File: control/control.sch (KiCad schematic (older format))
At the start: 135 parts, among them IC1 TJA1040, IC2 DNP MAX481CSA, IC3 ST232BD, IC4 ATMEGA128-A, IC5 ST232BD, IC6 FT232RL, J4 POWER, P1 SENSOR, P10 DB9, P11 B, P12 USB_4, P13 DB9, P2 I2C0, P3 I2C1, P4 I2C2, P5 COIN, P6 BILL, P7 ISP, P8 CONN_2, P9 CONN_2, X1 16MHz

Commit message: Updated control board for KiCad 4.0
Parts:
- removed P11: B, USB_B, symbol USB_B_5
- removed P12: USB_4, USB_MINI_B_6, symbol USB_MINI_B_6
- added P11: USB_B, Connect:USB_B, symbol USB_B
- added P12: USB_OTG, Connect:USB_Micro-B, symbol USB_OTG
- added R71: DNP, Resistors_SMD:R_0805_HandSoldering, symbol R
- C1, C10, C11, C12, C13, C14, C15, C16, C17, C18, C19, C2, C20, C21, C22, C23, C25, C27, C28, C29, C3, C30, C31, C4, C5, C6, C7, C8, C9: footprint R0805 -> Capacitors_SMD:C_0805_HandSoldering
- C24, C26, C32: footprint C1V5 -> Capacitors_ThroughHole:C_Radial_D5_L11_P2.5; symbol CP1 -> CP
- D1, D2, D3, D4, D5: footprint LED-0805 -> LEDs:LED-0805
- IC1, IC2: footprint SO8N -> Housings_SOIC:SOIC-8_3.9x4.9mm_Pitch1.27mm
- IC3, IC5: footprint SO16N -> Housings_SOIC:SOIC-16_3.9x9.9mm_Pitch1.27mm
- IC4: footprint TQFP64 -> Housings_QFP:TQFP-64_14x14mm_Pitch0.8mm
- IC6: footprint SSOP28 -> Housings_SSOP:SSOP-28_5.3x10.2mm_Pitch0.65mm
- J4: footprint he10-16ds -> Pin_Headers:Pin_Header_Straight_2x08; symbol BUS_I2C -> Bus_I2C
- JP1, JP2: footprint SIL-3 -> Pin_Headers:Pin_Header_Straight_1x03
- L1: footprint wuerth_elektronik_v5-WE-PD2_S -> matemat:wuerth_elektronik_v5-WE-PD2_S
- P1: footprint he10-16ds -> Pin_Headers:Pin_Header_Straight_2x08
- P10, P13: footprint DB9MCS -> matemat:DB9MCS
- P2, P3, P4, P5: footprint he10-10ds -> Pin_Headers:Pin_Header_Straight_2x05
- P6: footprint HE10_26DS -> Pin_Headers:Pin_Header_Straight_2x13
- P7: footprint pin_array_3x2 -> Pin_Headers:Pin_Header_Straight_2x03
- P8: value CONN_2 -> 12V; footprint Bornier_B2_Phoenix -> matemat:Bornier_B2_Phoenix
- P9: value CONN_2 -> 5V; footprint Bornier_B2_Phoenix -> matemat:Bornier_B2_Phoenix
- R1, R10, R11, R12, R13, R14, R15, R16, R17, R18, R19, R2, R20, R21, R22, R23, R24, R25, R26, R27, R28, R29, R3, R30, R31, R32, R33, R34, R35, R36, R37, R38, R39, R4, R40, R41, R42, R43, R44, R45, R46, R47, R48, R49, R5, R50, R51, R52, R53, R54, R55, R56, R57, R58, R59, R6, R60, R61, R62, R63, R64, R65, R66, R67, R68, R69, R7, R70, R8, R9: footprint R0805 -> Resistors_SMD:R_0805_HandSoldering
- TP1, TP2, TP3, TP4: footprint TROU3 -> Mounting_Holes:MountingHole_3mm
- X1: footprint Q_49U3HMS -> Crystals:Q_49U3HMS; symbol CRYSTAL -> Crystal
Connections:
- wire segments 296 -> 281
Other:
- moved on the sheet: C1, C10, C11, C12, C13, C14, C15, C16, C17, C18, C19, C2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

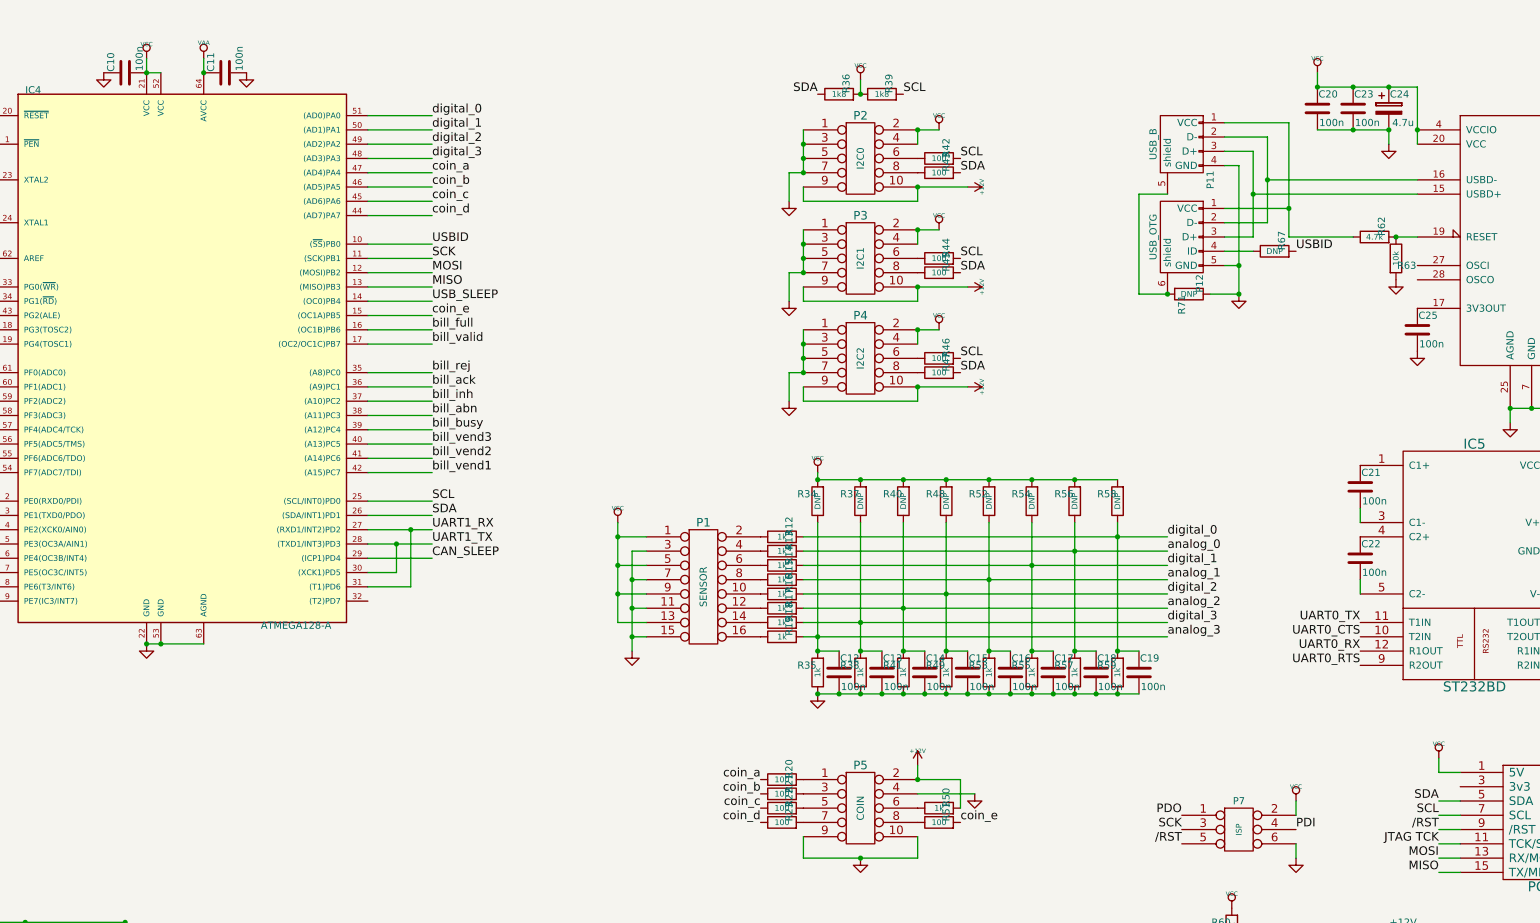
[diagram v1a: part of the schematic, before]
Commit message: Removed pulldown resistors from analog/digital I/O block to save some space. Removed leftover reference from conversion to KiCad 4.
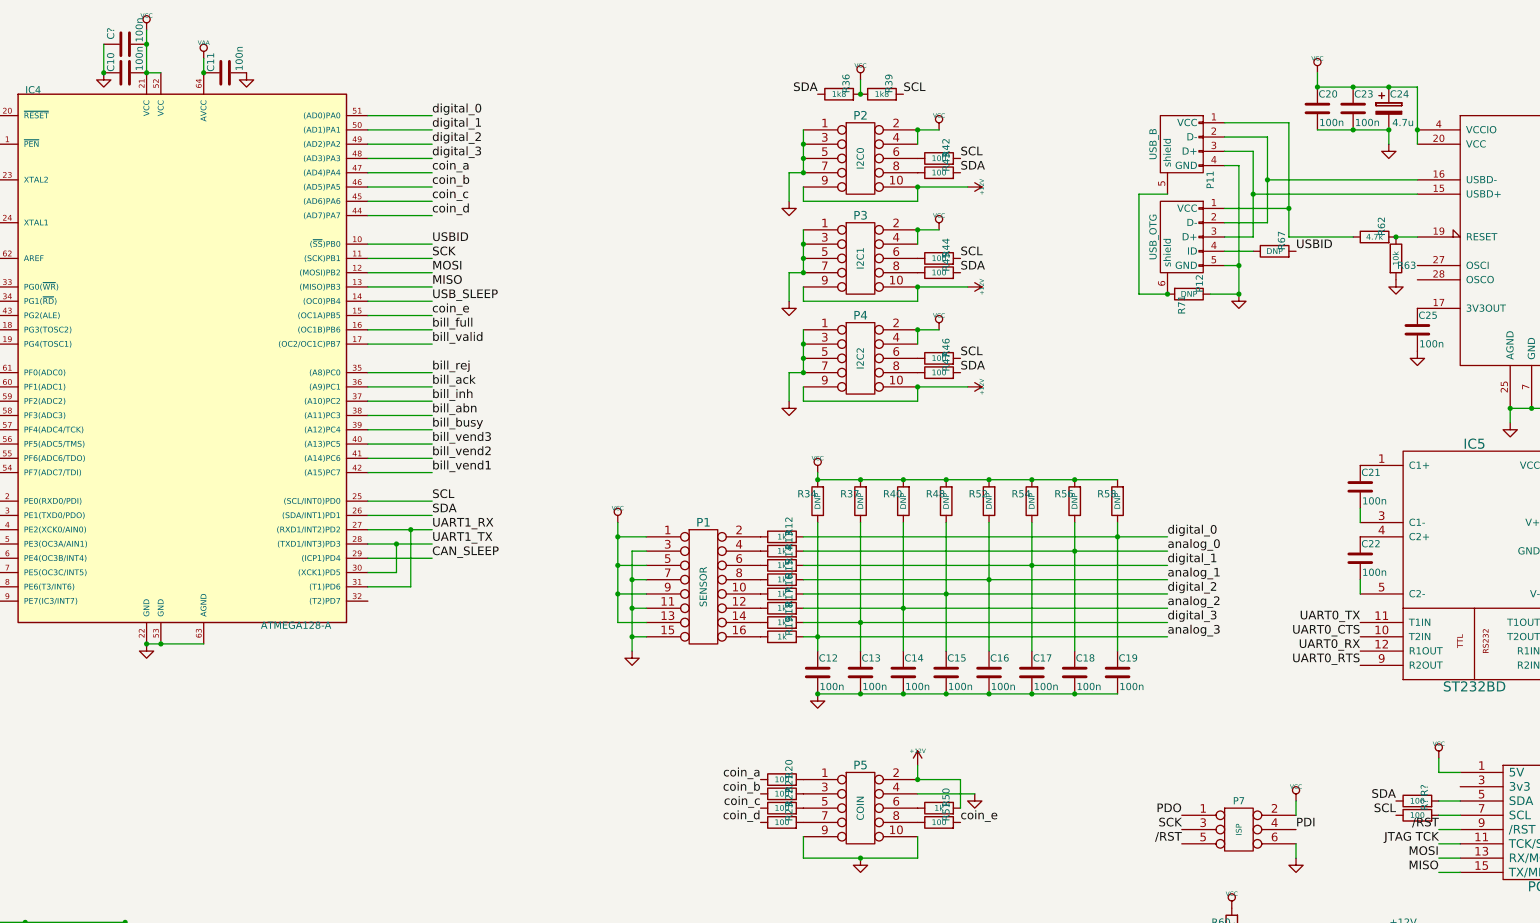
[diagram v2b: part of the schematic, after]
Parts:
- removed R35, R38, R41, R49, R53, R55, R57, R59: 1k, Resistors_SMD:R_0805_HandSoldering, symbol R
- added C?: 100n, Capacitors_SMD:C_0805_HandSoldering, symbol C
- added R? (x2): 100, Resistors_SMD:R_0805_HandSoldering, symbol R
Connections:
- net GND: now also C?.1
- net SCL: now also R?.1; no longer J4.7 (SCL)
- net SDA: now also R?.1; no longer J4.5 (SDA)
- net VCC: now also C?.2
- new net: J4.5 (SDA), R?.2
- new net: J4.7 (SCL), R?.2
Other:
- moved on the sheet: C12, C13, C14, C15, C16, C17, C18, C19

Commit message: Added new connection blocks for coin and banknote scanners
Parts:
- added P?: COIN, symbol CONN_01X17
- added P?: CONN_02X13, symbol CONN_02X13
- added R? (x13): 1k, Resistors_SMD:R_0805_HandSoldering, symbol R
- added R? (x4): 10k, Resistors_SMD:R_0805_HandSoldering, symbol R
- added R? (x2): DNP, Resistors_SMD:R_0805_HandSoldering, symbol R
- added R?: 0, Resistors_SMD:R_0805_HandSoldering, symbol R
- JP2: value 1-2 RESET -> RESET; symbol JUMPER3 -> JUMPER
- R61: value 1k -> 10k
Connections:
- net +12V: now also P?.1 (P1), P?.11 (P11), P?.3 (P3)
- net GND: now also P?.10 (P10), P?.12 (P12), P?.12 (P12), P?.14 (P14), P?.2 (P2), P?.22 (P22), P?.24 (P24), P?.26 (P26), P?.3 (P3), P?.4 (P4), P?.6 (P6), P?.8 (P8), R?.1, R?.1
- net VCC: now also P?.15 (P15), P?.17 (P17), P?.19 (P19), R?.2, R?.2, R?.2, R?.2, R?.2, R?.2, R?.2, R?.2, R?.2, R?.2, R?.2, R?.2, R?.2, R?.2, R?.2, R?.2, R?.2, R?.2
- net /RST renamed ~RST~
- net FLASH_EN renamed ~FLASH_EN~
- net analog_0 renamed ANALOG_0
- net analog_1 renamed ANALOG_1
- net analog_2 renamed ANALOG_2
- net analog_3 renamed ANALOG_3
- net digital_0 renamed DIGITAL_0
- net digital_1 renamed DIGITAL_1
- net digital_2 renamed DIGITAL_2
- net digital_3 renamed DIGITAL_3
- new net BILL_IN_ACK: P?.18 (P18), R?.1
- new net BILL_IN_INH: P?.16 (P16), R?.1
- new net BILL_IN_REJ: P?.20 (P20), R?.1
- new net BILL_OUT_ABN: P?.13 (P13), R?.1
- new net BILL_OUT_BUSY: P?.11 (P11), R?.1
- new net BILL_OUT_FULL: P?.23 (P23), R?.1
- new net BILL_OUT_VALID: P?.21 (P21), R?.1
- new net BILL_OUT_VEND1: P?.5 (P5), R?.1
- new net BILL_OUT_VEND2: P?.7 (P7), R?.1
- new net BILL_OUT_VEND3: P?.9 (P9), R?.1
- new net COIN_INH: P?.10 (P10), P?.13 (P13), P?.14 (P14), P?.15 (P15), P?.16 (P16), P?.17 (P17), R?.1, R?.2
- new net COIN_OUT_A: P?.1 (P1), R?.1
- new net COIN_OUT_B: P?.2 (P2), R?.1
- new net COIN_OUT_C: P?.9 (P9), R?.1
- new net COIN_OUT_D: P?.7 (P7), R?.1
- new net COIN_OUT_E: P?.6 (P6), R?.1
- new net COIN_OUT_F: P?.4 (P4), R?.1
- new net COIN_OUT_MODE: P?.8 (P8), R?.1, R?.2
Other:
- moved on the sheet: C13, C14, C15, C16, C17, C18, C19, JP1, P5, P6, R20, R21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

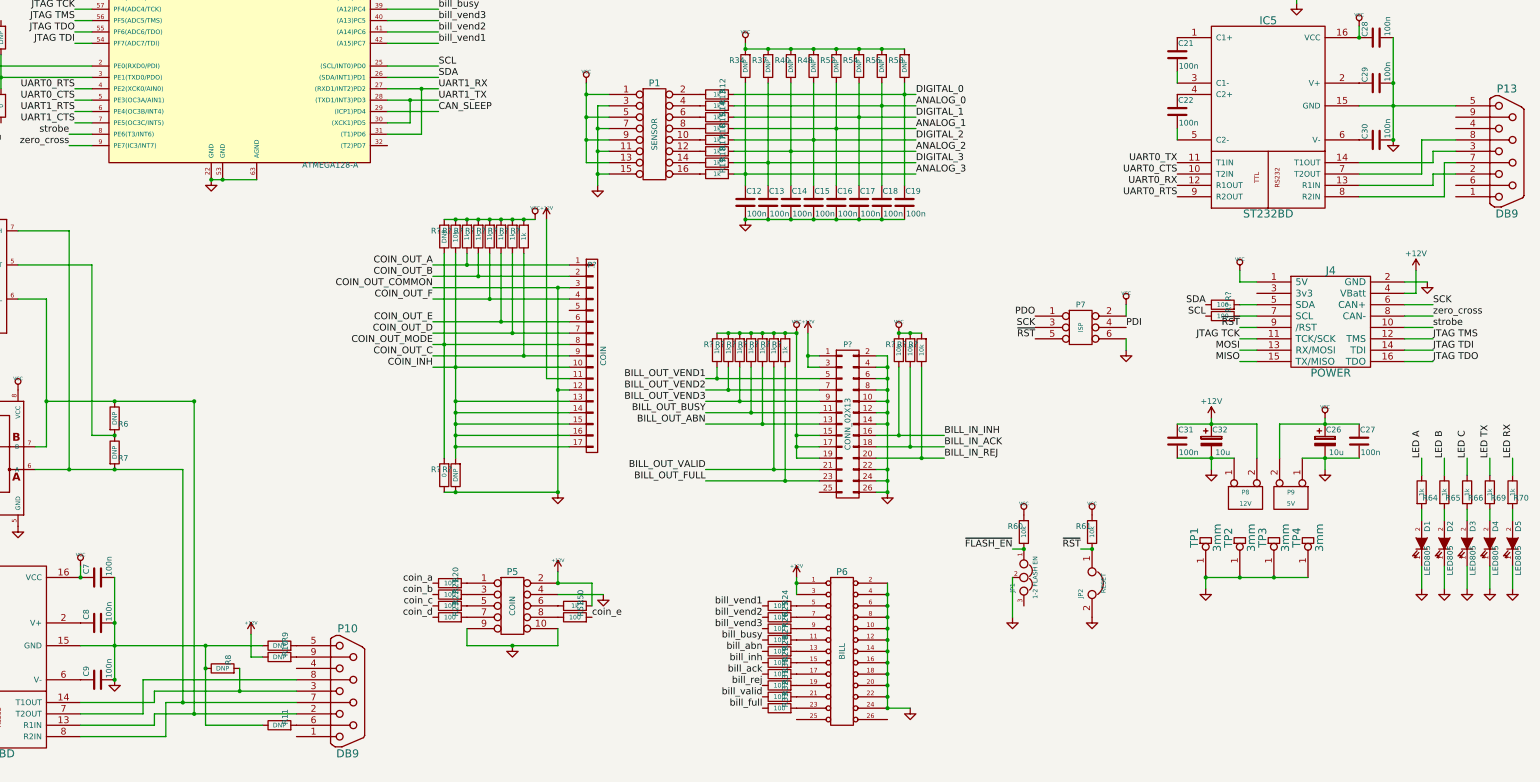
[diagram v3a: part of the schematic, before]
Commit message: Moved DB9 connectors in the schematic a little to clean up the trace mess
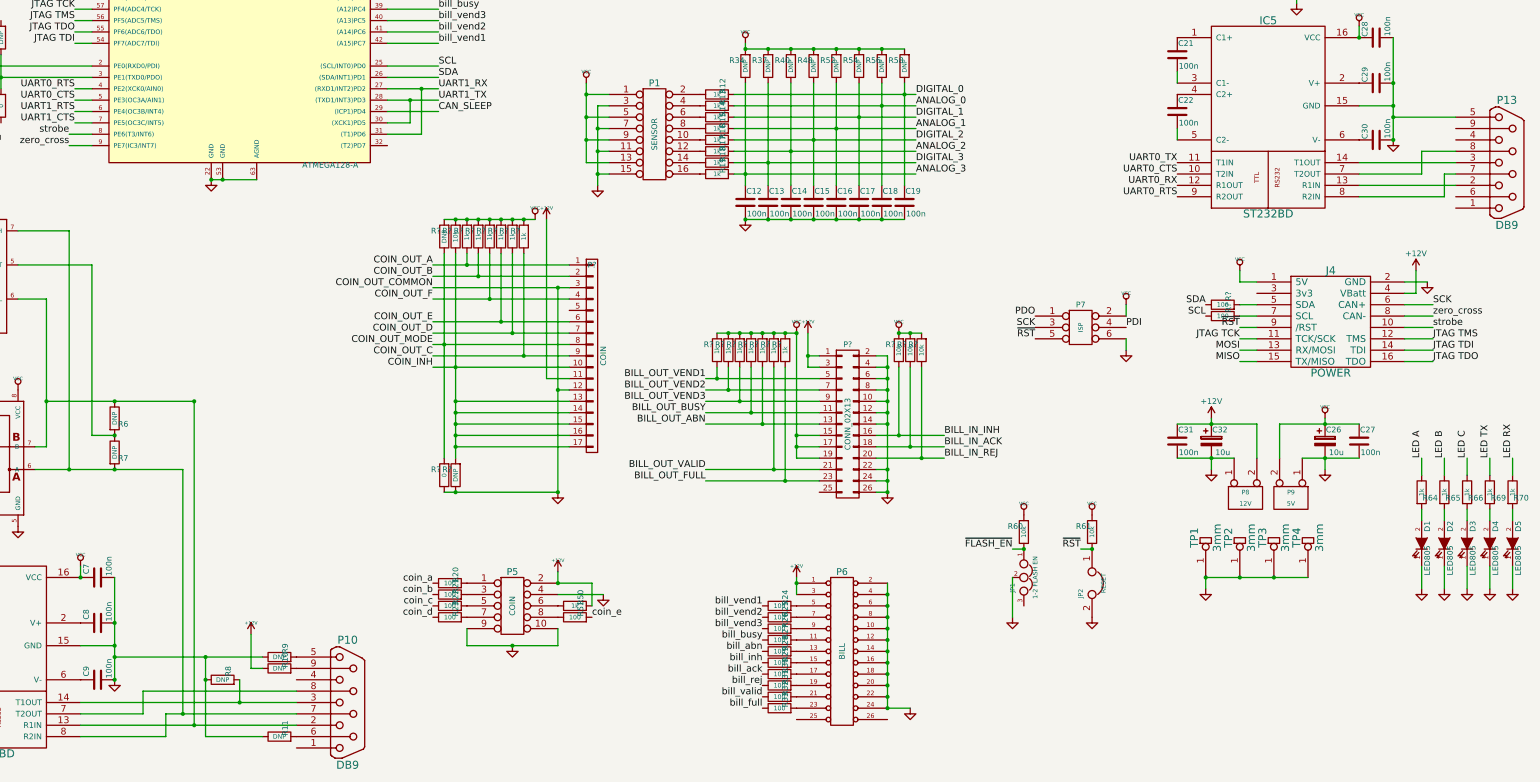
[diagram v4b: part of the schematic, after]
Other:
- moved on the sheet: P10, P13, R10, R11, R8, R9
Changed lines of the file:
@@
 L DB9 P13
 U 1 1 50A30577
-P 15650 5200
-F 0 "P13" H 15650 5750 70  0000 C CNN
-F 1 "DB9" H 15650 4650 70  0000 C CNN
-F 2 "matemat:DB9MCS" H 15650 5200 60  0001 C CNN
-F 3 "" H 15650 5200 60  0001 C CNN
-	1    15650 5200
+P 15650 5300
+F 0 "P13" H 15650 5850 70  0000 C CNN
+F 1 "DB9" H 15650 4750 70  0000 C CNN
+F 2 "matemat:DB9MCS" H 15650 5300 60  0001 C CNN
+F 3 "" H 15650 5300 60  0001 C CNN
+	1    15650 5300
 	1    0    0    -1
 $EndComp
@@
 L DB9 P10
 U 1 1 5116C3F6
-P 5450 9950
-F 0 "P10" H 5450 10500 70  0000 C CNN
-F 1 "DB9" H 5450 9400 70  0000 C CNN
-F 2 "matemat:DB9MCS" H 5450 9950 60  0001 C CNN
-F 3 "" H 5450 9950 60  0001 C CNN
-	1    5450 9950
+P 5450 10050
+F 0 "P10" H 5450 10600 70  0000 C CNN
+F 1 "DB9" H 5450 9500 70  0000 C CNN
+F 2 "matemat:DB9MCS" H 5450 10050 60  0001 C CNN
+F 3 "" H 5450 10050 60  0001 C CNN
+	1    5450 10050
 	1    0    0    -1
 $EndComp
@@
 L R R8
 U 1 1 5148CAB1
-P 4350 9750
-F 0 "R8" H 4425 9700 50  0000 C CNN
-F 1 "DNP" V 4350 9750 40  0000 C CNN
-F 2 "Resistors_SMD:R_0805_HandSoldering" H 4350 9750 60  0001 C CNN
-F 3 "" H 4350 9750 60  0001 C CNN
-	1    4350 9750
+P 4350 9850
+F 0 "R8" H 4425 9800 50  0000 C CNN
+F 1 "DNP" V 4350 9850 40  0000 C CNN
+F 2 "Resistors_SMD:R_0805_HandSoldering" H 4350 9850 60  0001 C CNN
+F 3 "" H 4350 9850 60  0001 C CNN
+	1    4350 9850
 	0    -1   -1   0
 $EndComp
@@
 L R R9
 U 1 1 5148CAC1
-P 4850 9550
-F 0 "R9" H 4925 9500 50  0000 C CNN
-F 1 "DNP" V 4850 9550 40  0000 C CNN
-F 2 "Resistors_SMD:R_0805_HandSoldering" H 4850 9550 60  0001 C CNN
-F 3 "" H 4850 9550 60  0001 C CNN
-	1    4850 9550
-	0    -1   -1   0
-$EndComp
-$Comp
-L R R10
-U 1 1 5148CAC7
 P 4850 9650
-F 0 "R10" H 4925 9600 50  0000 C CNN
+F 0 "R9" H 4925 9600 50  0000 C CNN
 F 1 "DNP" V 4850 9650 40  0000 C CNN
 F 2 "Resistors_SMD:R_0805_HandSoldering" H 4850 9650 60  0001 C CNN
@@
 $EndComp
 $Comp
+L R R10
+U 1 1 5148CAC7
+P 4850 9750
+F 0 "R10" H 4925 9700 50  0000 C CNN
+F 1 "DNP" V 4850 9750 40  0000 C CNN
+F 2 "Resistors_SMD:R_0805_HandSoldering" H 4850 9750 60  0001 C CNN
+F 3 "" H 4850 9750 60  0001 C CNN
+	1    4850 9750
+	0    -1   -1   0
+$EndComp
+$Comp
 L R R11
 U 1 1 5148CACD
-P 4850 10250
-F 0 "R11" H 4925 10200 50  0000 C CNN
-F 1 "DNP" V 4850 10250 40  0000 C CNN
-F 2 "Resistors_SMD:R_0805_HandSoldering" H 4850 10250 60  0001 C CNN
-F 3 "" H 4850 10250 60  0001 C CNN
-	1    4850 10250
+P 4850 10350
+F 0 "R11" H 4925 10300 50  0000 C CNN
+F 1 "DNP" V 4850 10350 40  0000 C CNN
+F 2 "Resistors_SMD:R_0805_HandSoldering" H 4850 10350 60  0001 C CNN
+F 3 "" H 4850 10350 60  0001 C CNN
+	1    4850 10350
 	0    -1   -1   0
 $EndComp
@@
 Wire Wire Line
 	2250 4450 2250 4650
-Connection ~ 4200 9550
+Connection ~ 4200 9650
 Wire Wire Line
-	4200 9550 4200 9750
+	4200 9650 4200 9850
 Wire Wire Line
-	4200 9750 4200 10250
-Connection ~ 4200 9750
-Connection ~ 4100 10150
+	4200 9850 4200 10350
+Connection ~ 4200 9850
+Connection ~ 4100 10250
 Wire Wire Line
 	2800 7400 3400 7400
@@
 	3400 7400 4100 7400
 Wire Wire Line
-	4100 7400 4100 10150
+	4100 7400 4100 10250
 Wire Wire Line
 	3000 5900 2550 5900
 Connection ~ 3400 8000
-Wire Wire Line
-	4200 10250 4700 10250
-Connection ~ 4000 10050
+Connection ~ 4000 10150
 Connection ~ 3000 8000
 Wire Wire Line
-	4000 8000 4000 10050
-Wire Wire Line
-	4600 9650 4600 9450
+	4000 8000 4000 10150
 Wire Wire Line
-	4700 9650 4600 9650
+	4600 9750 4600 9450
 Wire Wire Line
 	11400 8700 11300 8700
@@
 	3100 8850 3100 8950
 Wire Wire Line
-	3100 9550 3400 9550
+	3400 9550 3100 9550
 Wire Wire Line
-	3400 9550 4200 9550
+	3400 9650 4200 9650
 Wire Wire Line
-	4200 9550 4700 9550
+	4200 9650 4700 9650
 Wire Wire Line
 	3100 10350 3850 10350
 Wire Wire Line
-	3100 10250 3750 10250
-Wire Wire Line
-	3100 10150 3650 10150
-Wire Wire Line
-	3100 10050 3750 10050
-Wire Wire Line
-	3850 10050 4000 10050
+	3100 10250 4100 10250
 Wire Wire Line
-	4000 10050 5000 10050
+	4100 10250 5000 10250
 Wire Wire Line
-	3850 10350 3850 10050
-Wire Wire Line
-	3650 9850 5000 9850
+	3100 10150 3650 10150
 Wire Wire Line
-	3650 10150 3650 9850
+	3100 10050 4500 10050
 Wire Wire Line
-	3750 9950 4500 9950
+	4500 10050 5000 10050
 Wire Wire Line
-	4500 9950 5000 9950
+	3850 10150 4000 10150
 Wire Wire Line
-	3750 10050 3750 9950
+	4000 10150 5000 10150
 Wire Wire Line
-	3750 10150 4100 10150
+	3850 10350 3850 10150
 Wire Wire Line
-	4100 10150 5000 10150
+	3650 9950 5000 9950
 Wire Wire Line
-	3750 10250 3750 10150
+	3650 10150 3650 9950
 Connection ~ 3400 9350
 Connection ~ 3400 9550
@@
 	3400 9350 3400 9550
 Wire Wire Line
-	3400 9550 3400 9850
+	3400 9550 3400 9650
+Wire Wire Line
+	3400 9650 3400 9850
 Wire Wire Line
 	3050 4750 3200 4750
@@
 	14350 4100 14350 4200
 Wire Wire Line
-	14350 4800 14650 4800
-Wire Wire Line
-	14650 4800 15200 4800
+	14650 4900 15200 4900
 Wire Wire Line
 	14350 5600 15100 5600
 Wire Wire Line
-	14350 5500 15000 5500
+	14350 5500 15200 5500
 Wire Wire Line
 	14350 5400 14900 5400
 Wire Wire Line
-	14350 5300 15000 5300
-Wire Wire Line
-	15100 5300 15200 5300
-Wire Wire Line
-	15100 5600 15100 5300
-Wire Wire Line
-	14900 5100 15200 5100
+	14350 5300 15200 5300
 Wire Wire Line
-	14900 5400 14900 5100
+	15100 5400 15200 5400
 Wire Wire Line
-	15000 5200 15200 5200
+	15100 5600 15100 5400
 Wire Wire Line
-	15000 5300 15000 5200
+	14900 5200 15200 5200
 Wire Wire Line
-	15000 5400 15200 5400
-Wire Wire Line
-	15000 5500 15000 5400
+	14900 5400 14900 5200
 Connection ~ 14650 4600
-Connection ~ 14650 4800
+Connection ~ 14650 4900
 Wire Wire Line
 	14650 4200 14650 4600
@@
 	14650 4600 14650 4800
 Wire Wire Line
-	14650 4800 14650 5100
+	14650 4800 14650 4900
+Wire Wire Line
+	14650 4900 14650 5100
 Connection ~ 14250 3800
 Wire Wire Line
@@
 Connection ~ 3400 7400
 Wire Wire Line
-	4500 9750 4500 9950
-Connection ~ 4500 9950
+	4500 10050 4500 9850
+Connection ~ 4500 10050
 Wire Wire Line
 	11400 3000 11200 3000
@@
 Connection ~ 6300 6900
 Connection ~ 6400 8200
+Wire Wire Line
+	14350 4800 14650 4800
+Connection ~ 14650 4800
+Connection ~ 3400 9650
+Wire Wire Line
+	4600 9750 4700 9750
+Wire Wire Line
+	4200 10350 4700 10350
 $EndSCHEMATC
